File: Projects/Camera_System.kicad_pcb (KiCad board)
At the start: 2 copper layers, 219.3 x 160.9 mm, 60 parts, among them CON1 AVR-ISP-10, J1 BARREL_JACK, U1 IFX1117ME_V33, U10 RT1105AF160Q, U11 RT1105AF160Q, U12 LCD_1602, U13 RT1105AF160Q, U14 Si501, U15 OV7670-nofifo, U16 ESP8266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

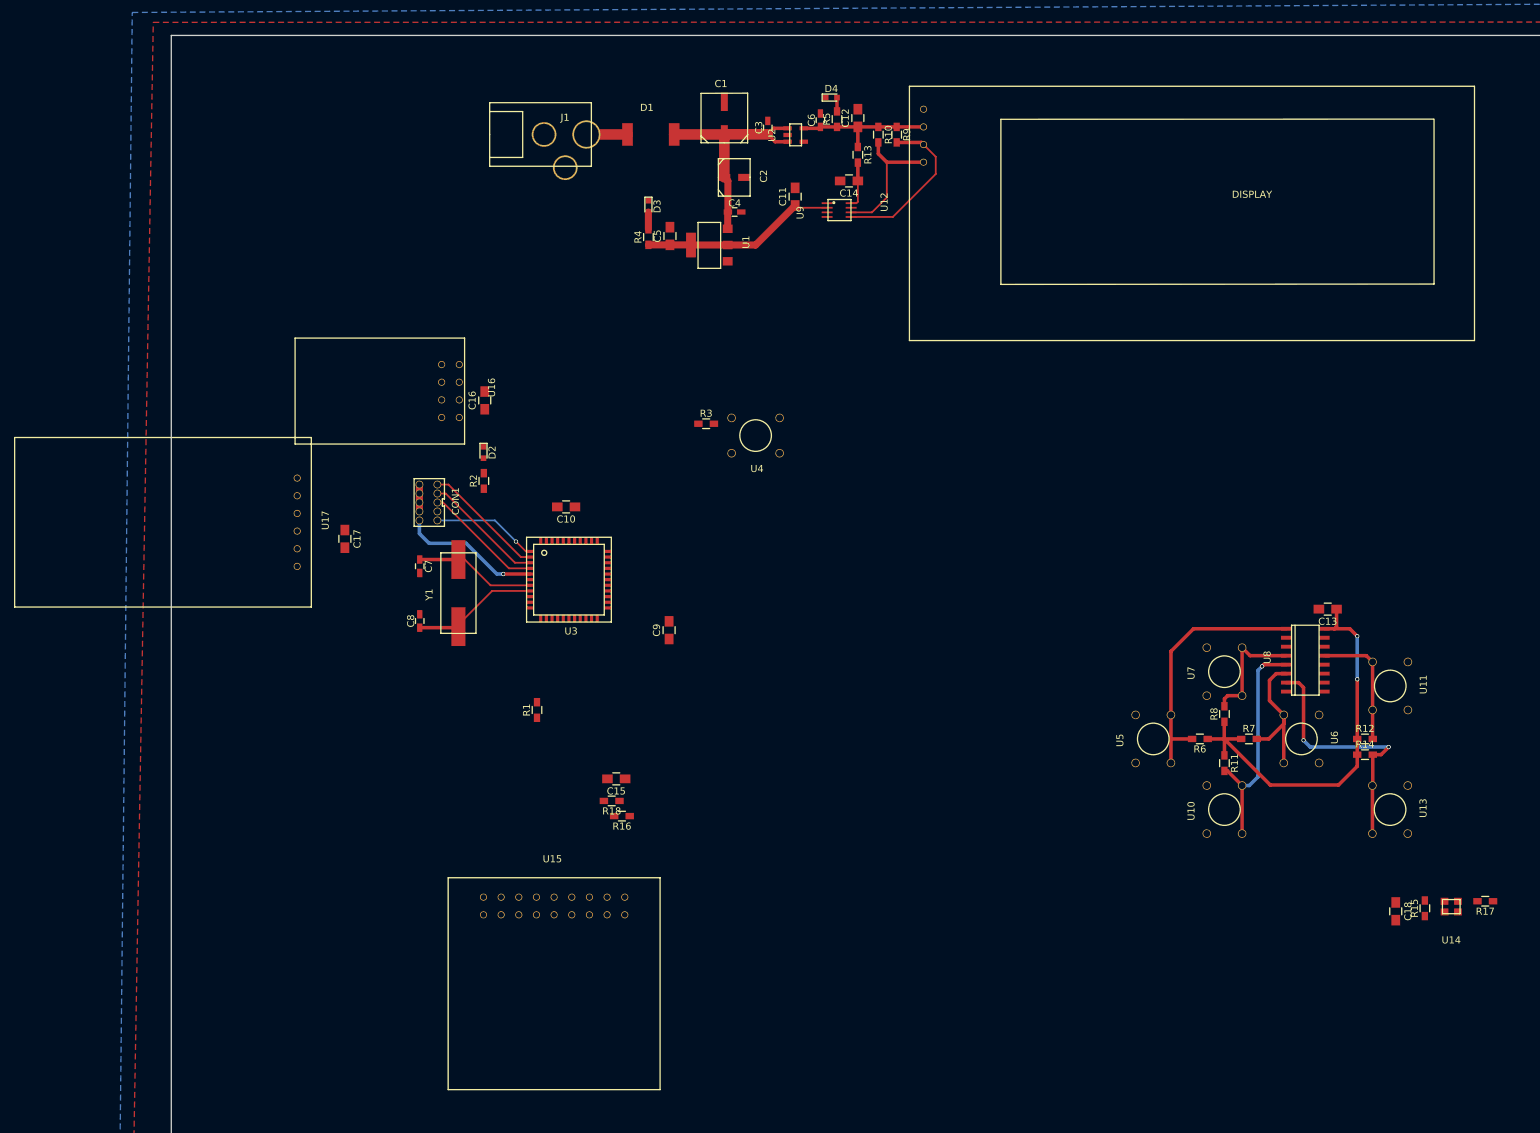
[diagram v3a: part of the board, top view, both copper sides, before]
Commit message: Layout has been updated
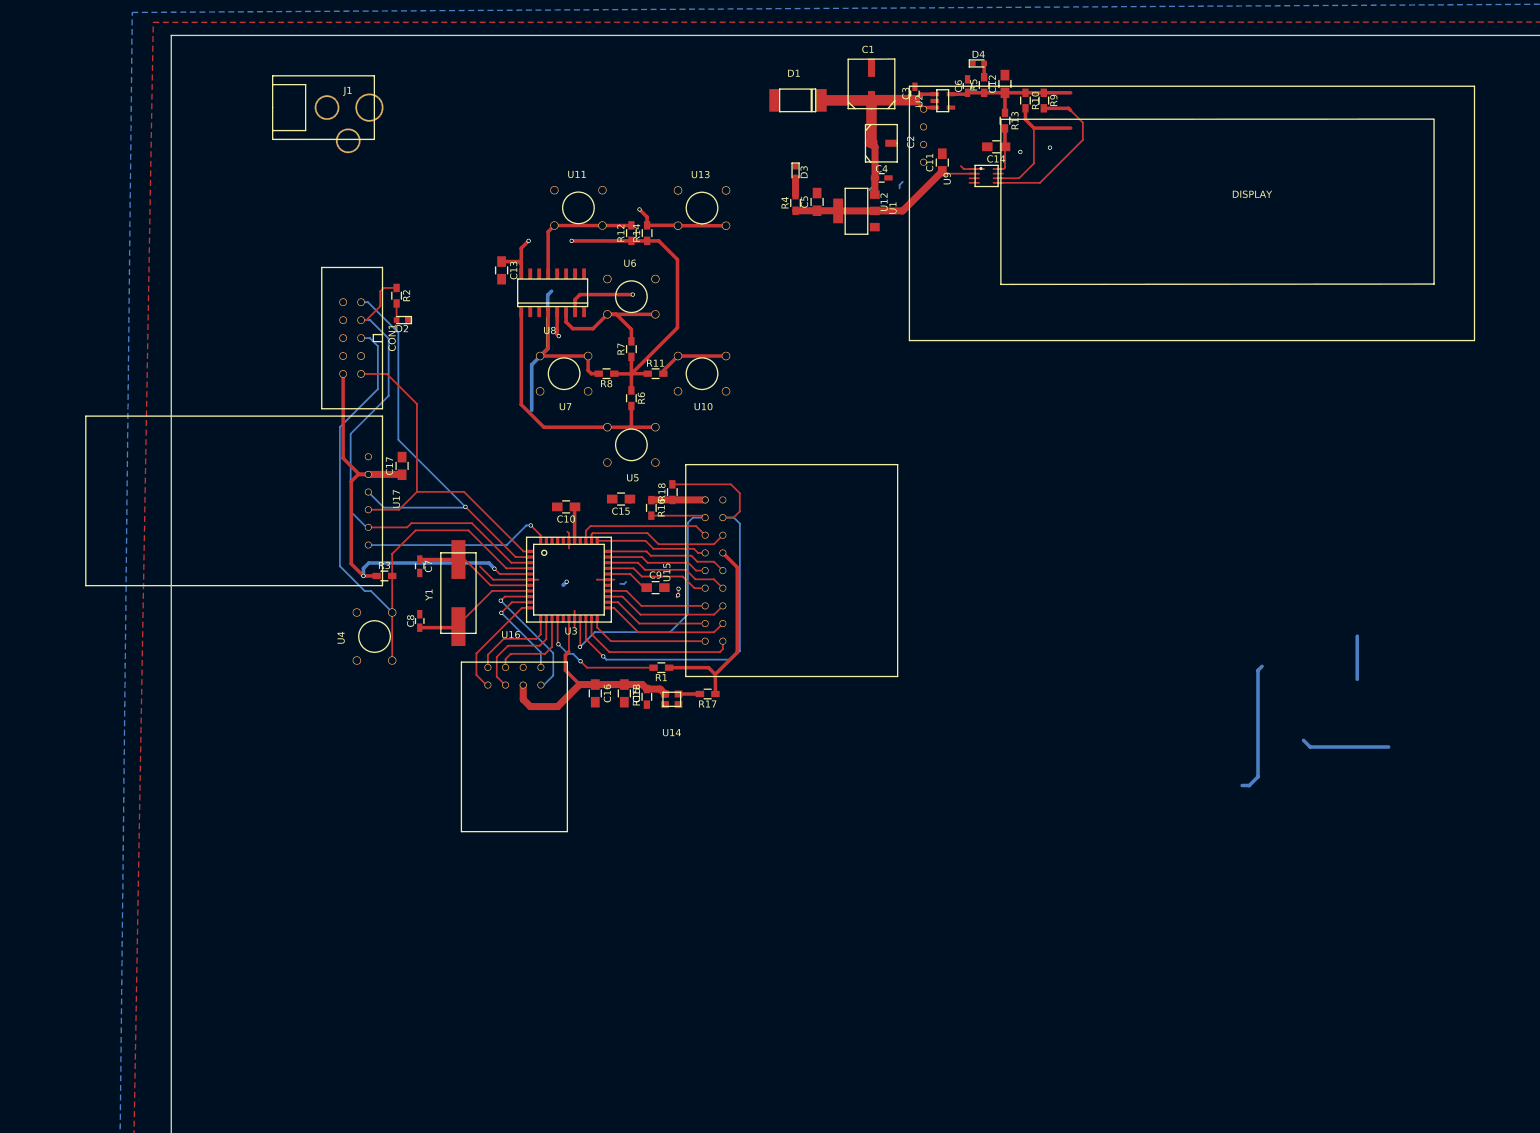
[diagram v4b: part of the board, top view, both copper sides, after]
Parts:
- moved U11 133.4 mm to (110.0, 53.8), turned to 180 degrees
- moved U13 129.4 mm to (127.5, 53.8), turned to 180 degrees
- moved C13 126.4 mm to (99.2, 62.7), turned to 270 degrees
- moved R12 126.2 mm to (117.5, 57.4), turned to 90 degrees
- moved R14 125.6 mm to (119.8, 57.4), turned to 90 degrees
- moved U8 118.6 mm to (106.4, 65.8), turned to 0 degrees
- moved U14 114.2 mm to (123.3, 123.4)
- moved R15 114.1 mm to (119.7, 123.0)
- moved R17 113.9 mm to (128.3, 122.6)
- moved U6 113.7 mm to (117.5, 66.4), turned to 180 degrees
- moved C18 113.5 mm to (116.5, 122.5)
- moved R7 103.4 mm to (117.5, 73.8), turned to 90 degrees
- moved U7 102.6 mm to (108.0, 77.3), turned to 0 degrees
- moved R8 99.9 mm to (114.0, 77.3), turned to 180 degrees
- moved R11 97.6 mm to (121.0, 77.3), turned to 0 degrees
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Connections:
- U3 pad 11: /CAM_RST -> /WLAN_RST
- U3 pad 12: /CAM_PWDN -> /WLAN_GPIO2
- U3 pad 13: /CAM_D1 -> /WLAN_GPIO0
- U3 pad 14: /P_S_CLK -> /WLAN_CHPD
- U3 pad 15: /CAM_HREF -> Net-(R1-Pad2)
- U3 pad 16: /CAM_VSINC -> (no net)
- U3 pad 21: /WLAN_CHPD -> /CAM_PWDN
- U3 pad 22: /WLAN_RST -> /CAM_RST
- U3 pad 23: /WLAN_GPIO0 -> /CAM_D0
- U3 pad 24: /WLAN_GPIO2 -> /CAM_D1
- U3 pad 25: (no net) -> /CAM_D2
- U3 pad 26: (no net) -> /CAM_D3
- U3 pad 30: /CAM_D7 -> /CAM_D5
- U3 pad 31: /CAM_D6 -> /CAM_D4
- U3 pad 32: /CAM_D5 -> /CAM_D7
- U3 pad 33: /CAM_D4 -> /CAM_D6
- U3 pad 34: /CAM_D3 -> /CAM_PCLK
- U3 pad 35: /CAM_D2 -> /CAM_HREF
- U3 pad 36: /CAM_PCLK -> /CAM_VSINC
- U3 pad 37: /CAM_D0 -> (no net)
- U3 pad 43: Net-(R1-Pad2) -> /P_S_CLK
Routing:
- net +3V3: track 106.2 -> 193.3 mm, vias 3 -> 4
- net /MIC_RST: track 17.0 -> 84.6 mm
- net /3V3_SDA: track 0.00 -> 62.6 mm, vias 0 -> 1
- net (no net): track 0.00 -> 60.1 mm, vias 0 -> 5
- net /SCK: track 17.2 -> 68.7 mm
- net /3V3_SCL: track 0.00 -> 45.1 mm, vias 0 -> 1
- net /MISO: track 18.4 -> 62.9 mm, vias 0 -> 1
- net /MOSI: track 14.9 -> 49.5 mm, vias 1 -> 0
- net /CAM_XCLK: track 0.00 -> 29.0 mm
- net /SDC_CS: track 0.00 -> 26.9 mm, vias 0 -> 1
- net /CAM_PWDN: track 0.00 -> 23.2 mm
- net /CAM_HREF: track 0.00 -> 20.8 mm
- net /WLAN_RX: track 0.00 -> 20.4 mm, vias 0 -> 1
- net /CAM_VSINC: track 0.00 -> 19.1 mm
- net /CTRL_DOWN: track 32.3 -> 13.7 mm
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
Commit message: Layout first draft finished
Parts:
- added U18: header_male_2.54_2x2, MyLibraries:header_male_2.54_2x2, F.Cu at (88.3, 125.3)
- added U19: header_male_2.54_2x2, MyLibraries:header_male_2.54_2x2, F.Cu at (88.3, 119.7)
- added U20: header_male_2.54_2x3, MyLibraries:header_male_2.54_2x3, F.Cu at (92.7, 87.4)
- moved C4 61.9 mm to (91.1, 50.1), turned to 180 degrees
- moved C3 61.1 mm to (96.9, 43.4), turned to 180 degrees
- moved C2 59.6 mm to (92.0, 47.7), turned to 270 degrees
- moved R9 59.0 mm to (116.9, 38.8), turned to 0 degrees
- moved C12 58.8 mm to (111.7, 38.8), turned to 180 degrees
- moved U2 58.2 mm to (102.8, 46.9)
- moved C6 57.7 mm to (108.0, 45.0)
- moved U1 57.7 mm to (94.3, 53.0), turned to 180 degrees
- moved D3 57.6 mm to (84.0, 58.6), turned to 0 degrees
- moved R10 56.5 mm to (116.9, 41.6), turned to 0 degrees
- moved R5 55.3 mm to (113.1, 46.1), turned to 0 degrees
- moved C1 53.6 mm to (97.9, 39.6)
- moved R4 52.9 mm to (88.2, 58.6), turned to 180 degrees
- moved D1 51.9 mm to (92.6, 39.6)
- moved C5 51.4 mm to (93.0, 61.2), turned to 180 degrees
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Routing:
- net +3V3: track 193.3 -> 399.5 mm, vias 4 -> 9
- net /3V3_SDA: track 62.6 -> 152.1 mm, vias 1 -> 2
- net /3V3_SCL: track 45.1 -> 133.4 mm, vias 1 -> 2
- net /P_S_CTRL: track 0.00 -> 48.4 mm, vias 0 -> 2
- net /P_S_CLK: track 0.00 -> 48.4 mm, vias 0 -> 2
- net /SERIAL_IN: track 0.00 -> 41.4 mm, vias 0 -> 2
- net (no net): track 60.1 -> 91.6 mm, vias 5 -> 27
- net /SCK: track 68.7 -> 92.6 mm
- net /CTRL_DOWN: track 13.7 -> 31.2 mm
- net /SDC_CS: track 26.9 -> 44.4 mm
- net GND: track 21.4 -> 37.9 mm, vias 0 -> 6
- net /WLAN_TX: track 14.7 -> 31.1 mm
- net /WLAN_RX: track 20.4 -> 36.1 mm
- net /CTRL_BTN2: track 24.1 -> 36.5 mm
- net +5V: track 19.9 -> 30.9 mm
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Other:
- board size 219.3 x 160.9 mm -> 67 x 98 mm
- board text added: "MISO"
- board text added: "MOSI"
- board text added: "RX"
- board text added: "SCK"
- board text added: "SCL"
- board text added: "SDA"
- board text added: "TX"

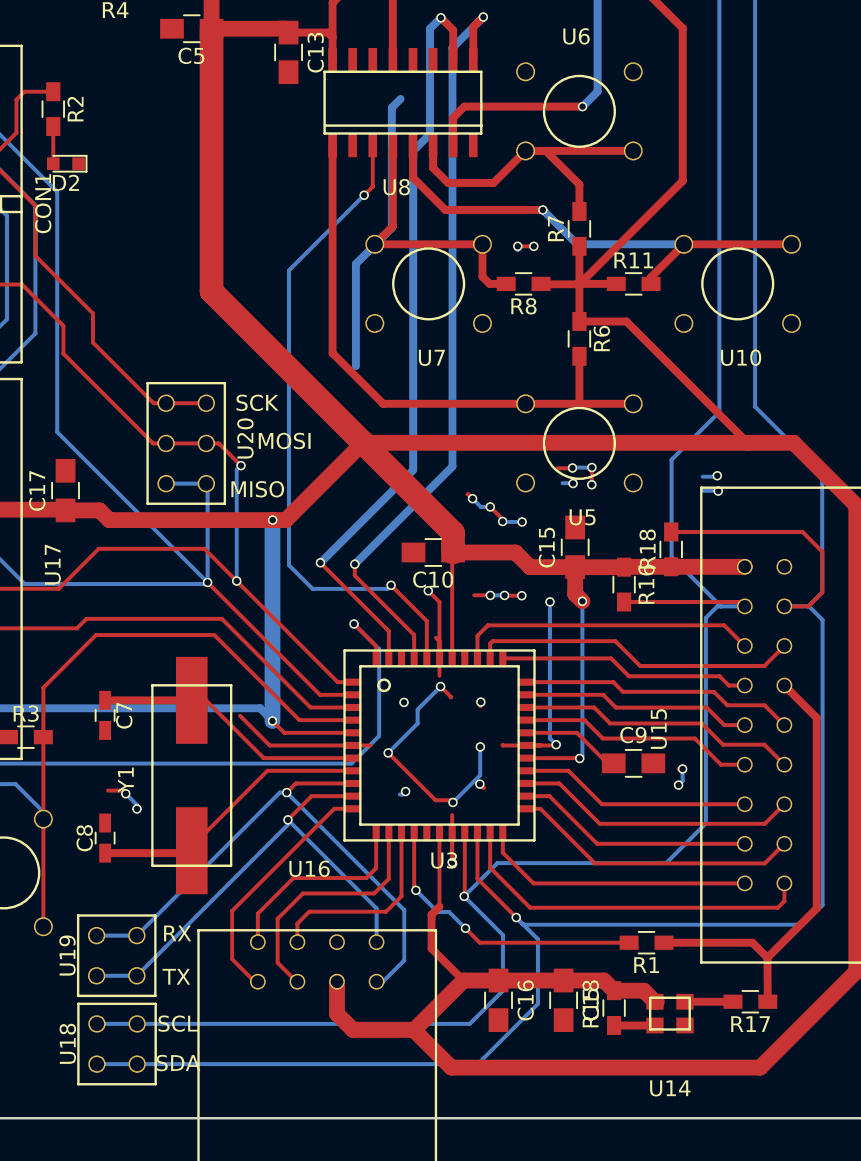
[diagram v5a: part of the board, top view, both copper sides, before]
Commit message: Layout has been reviewed and there are no electric problems with it
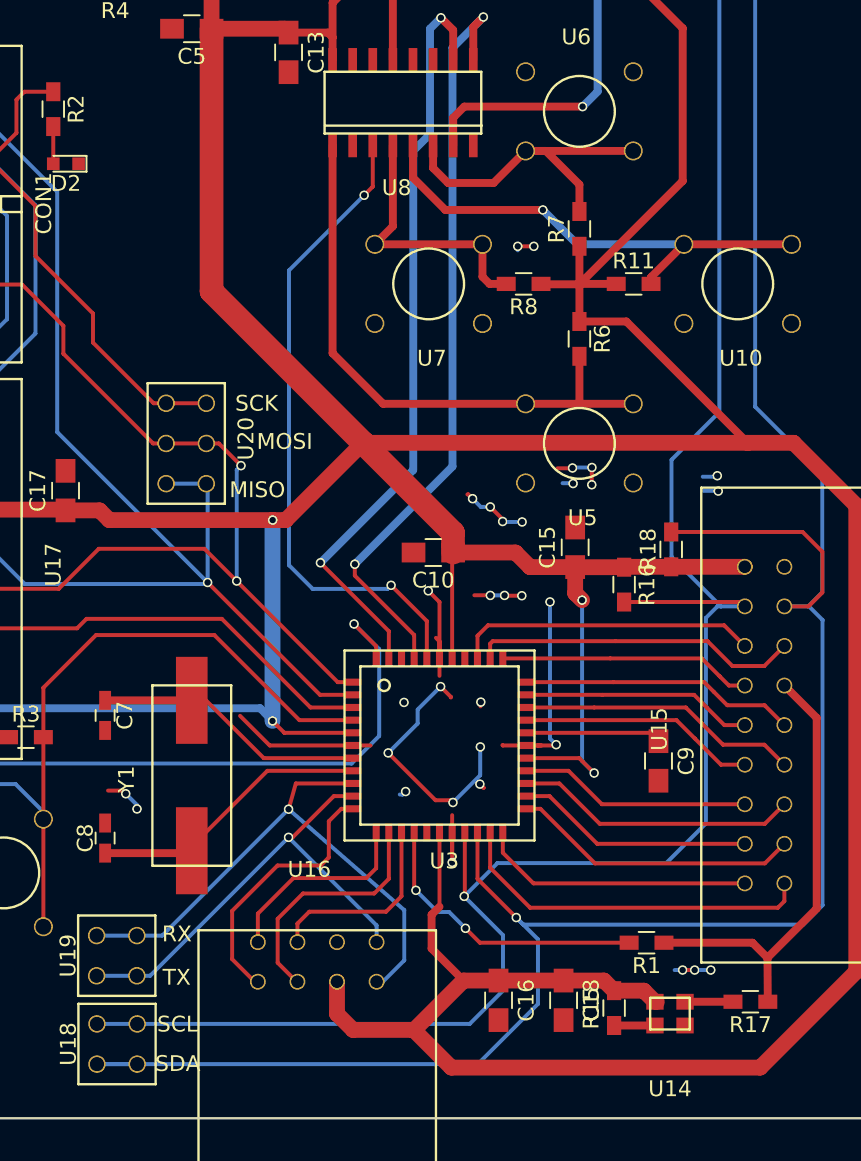
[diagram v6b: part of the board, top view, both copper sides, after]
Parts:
- moved C9 1.58 mm to (122.5, 107.4), turned to 270 degrees
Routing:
- net (no net): track 91.6 -> 75.9 mm, vias 27 -> 30
- net /3V3_SDA: track 152.1 -> 154.6 mm
- net +3V3: track 399.5 -> 401.9 mm
- net Net-(C9-Pad1): track 6.31 -> 8.55 mm
- net /WLAN_RST: track 15.5 -> 16.9 mm
- net GND: track 37.9 -> 36.6 mm, vias 6 -> 4
- net /WLAN_TX: track 31.1 -> 29.8 mm
